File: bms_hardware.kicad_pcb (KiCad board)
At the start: 2 copper layers, 102 parts, among them J1 Conn_01x05_Male, J2 Conn_01x07_Female, Q1 2N7002, Q2 2N7002, Q3 2N7002, Q4 2N7002, Q5 2N7002, Q6 2N7002, U1 STM32F407VGTx, U2 BQ76PL536A, U3 INA226, Y1 8MHz

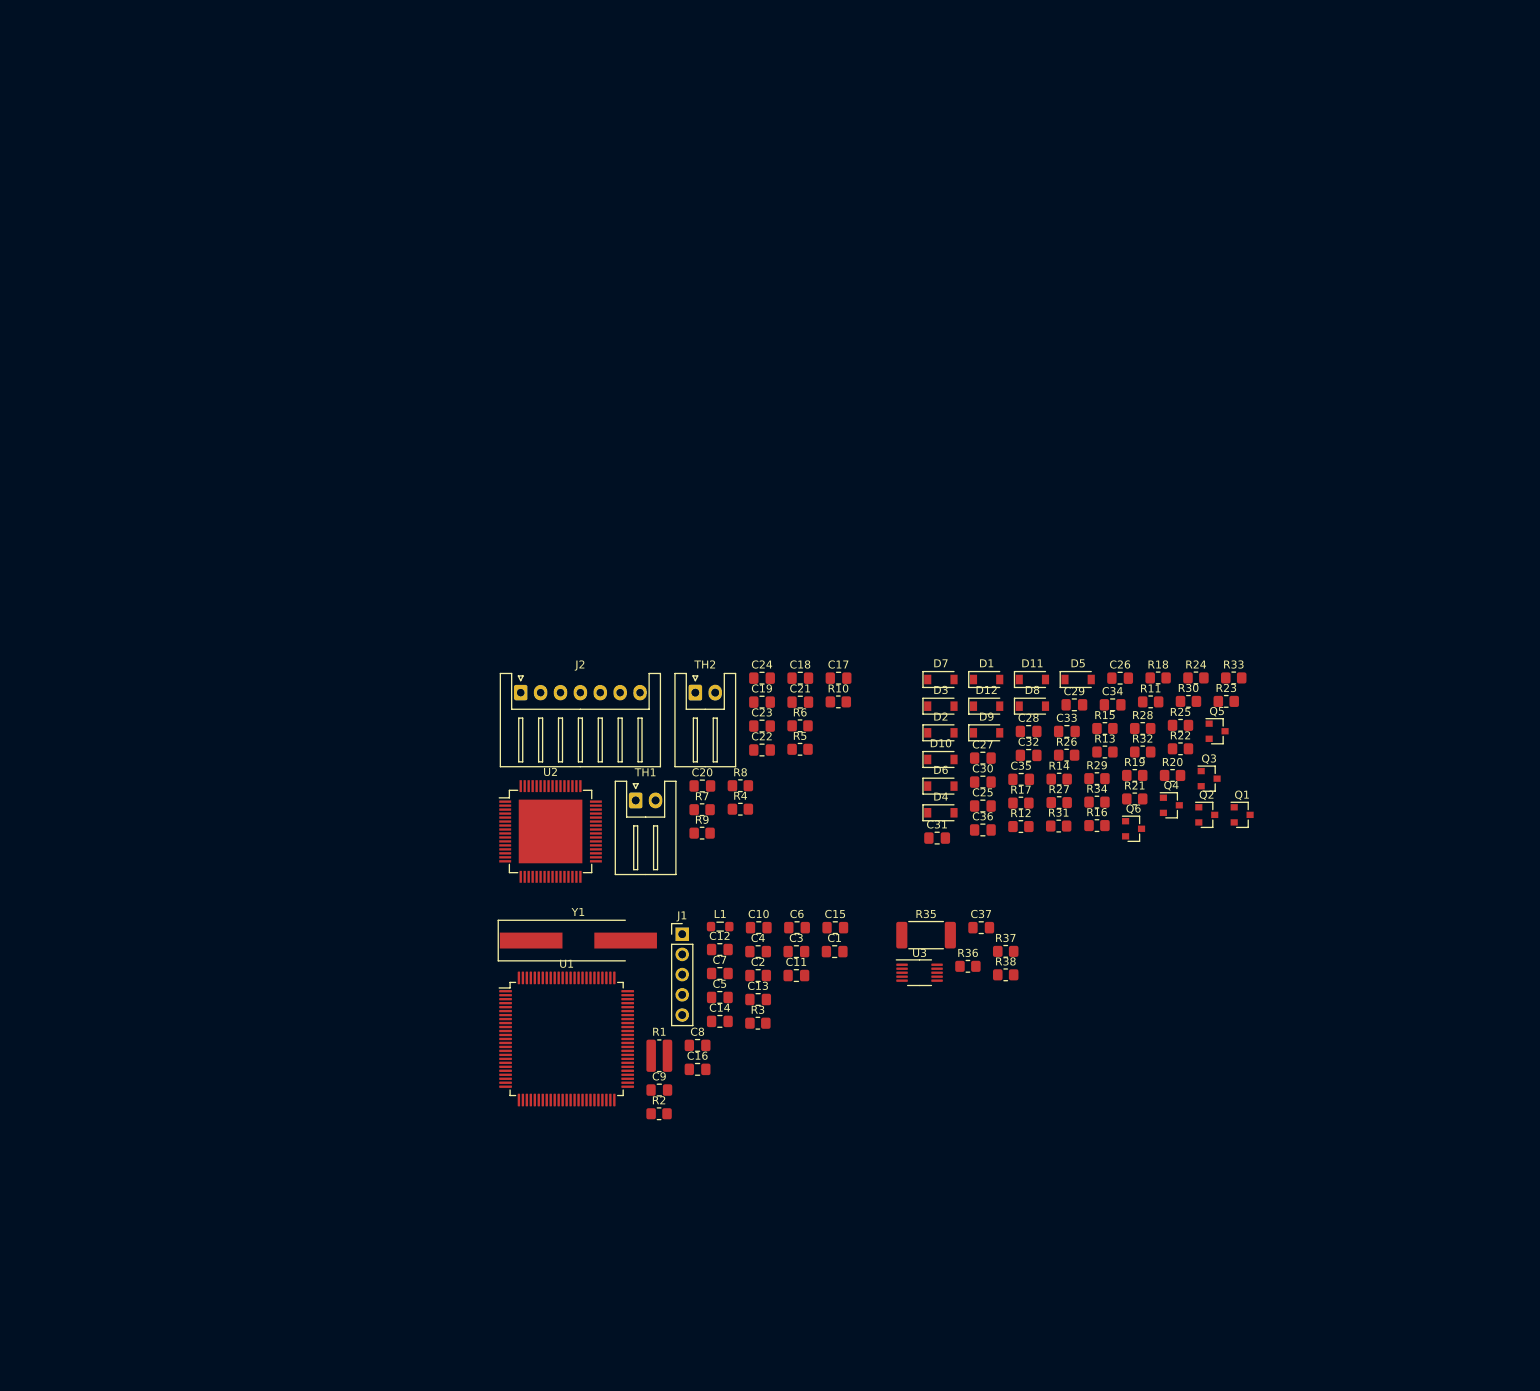
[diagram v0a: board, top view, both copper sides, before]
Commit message: Fixes missing footprints, adds initial pcb
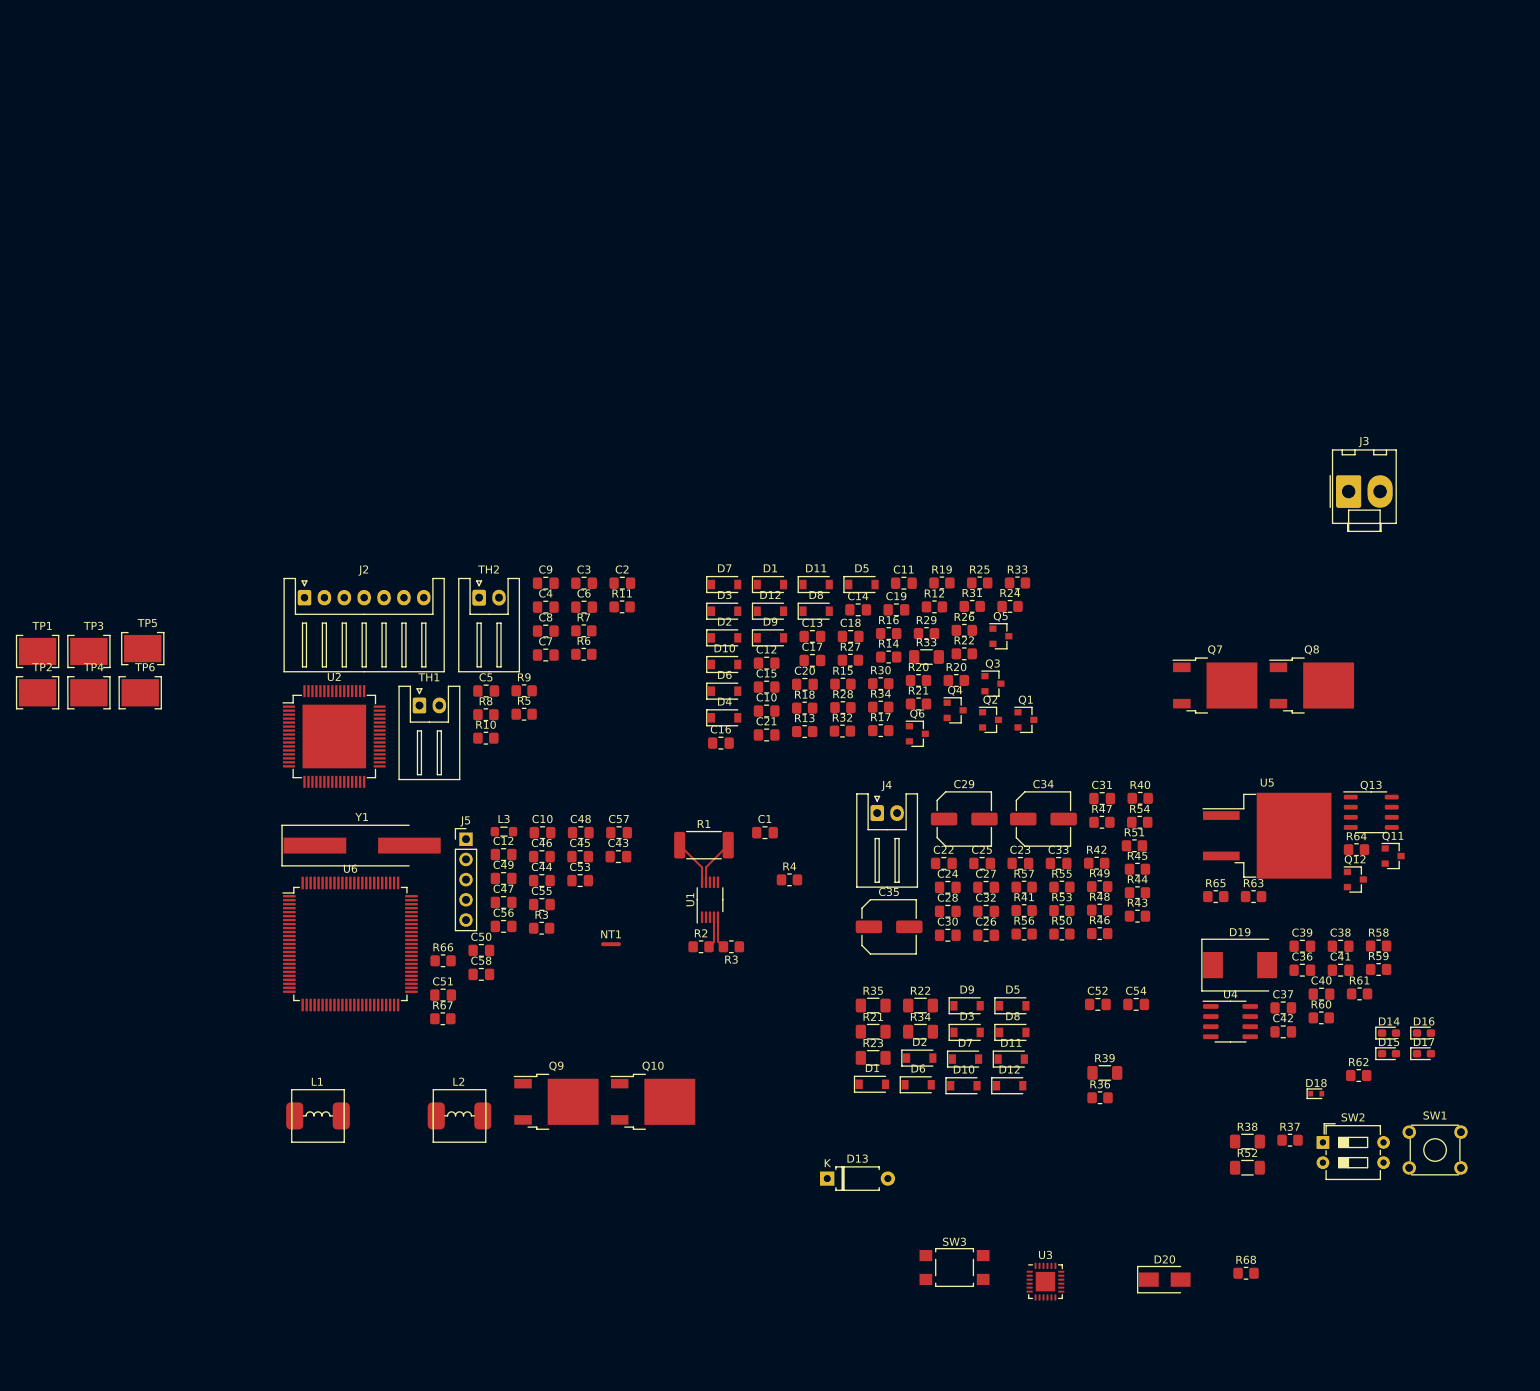
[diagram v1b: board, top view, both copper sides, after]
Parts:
- removed the R1 at (137.1, 113.1)
- removed the R32 at (197.9, 74.9)
- added C22: 1uF, Capacitor_SMD:C_0805_2012Metric_Pad1.18x1.45mm_HandSolder, F.Cu at (172.9, 88.9)
- added C23: 1uF, Capacitor_SMD:C_0805_2012Metric_Pad1.18x1.45mm_HandSolder, F.Cu at (182.5, 88.9)
- added C24: 2.7nF, Capacitor_SMD:C_0805_2012Metric_Pad1.18x1.45mm_HandSolder, F.Cu at (173.4, 91.9)
- added C25: 0.1uF, Capacitor_SMD:C_0805_2012Metric_Pad1.18x1.45mm_HandSolder, F.Cu at (177.7, 88.9)
- added C26: 0.1uF, Capacitor_SMD:C_0805_2012Metric_Pad1.18x1.45mm_HandSolder, F.Cu at (178.2, 97.9)
- added C27: 0.1uF, Capacitor_SMD:C_0805_2012Metric_Pad1.18x1.45mm_HandSolder, F.Cu at (178.2, 91.9)
- added C28: 0.056uF, Capacitor_SMD:C_0805_2012Metric_Pad1.18x1.45mm_HandSolder, F.Cu at (173.4, 94.9)
- added C29: 10uF, Capacitor_SMD:C_Elec_6.3x7.7, F.Cu at (175.5, 83.3)
- added C30: 1uF, Capacitor_SMD:C_0805_2012Metric_Pad1.18x1.45mm_HandSolder, F.Cu at (173.4, 97.9)
- added C31: 0.1uF, Capacitor_SMD:C_0805_2012Metric_Pad1.18x1.45mm_HandSolder, F.Cu at (192.8, 80.8)
- added C32: 0.1uF, Capacitor_SMD:C_0805_2012Metric_Pad1.18x1.45mm_HandSolder, F.Cu at (178.2, 94.9)
- added C33: 0.1uF, Capacitor_SMD:C_0805_2012Metric_Pad1.18x1.45mm_HandSolder, F.Cu at (187.3, 88.9)
- added C34: 10uF, Capacitor_SMD:C_Elec_6.3x7.7, F.Cu at (185.4, 83.3)
- added C35: 10uF, Capacitor_SMD:C_Elec_6.3x7.7, F.Cu at (166.0, 96.9)
- added C36: 3.3nF, Capacitor_SMD:C_0805_2012Metric_Pad1.18x1.45mm_HandSolder, F.Cu at (218.0, 102.3)
- added C37: 330nF, Capacitor_SMD:C_0805_2012Metric_Pad1.18x1.45mm_HandSolder, F.Cu at (215.6, 107.1)
- added C38: 10uF, Capacitor_SMD:C_0805_2012Metric_Pad1.18x1.45mm_HandSolder, F.Cu at (222.8, 99.3)
- added C39: 0.1uF, Capacitor_SMD:C_0805_2012Metric_Pad1.18x1.45mm_HandSolder, F.Cu at (218.0, 99.3)
- added C40: 2.2nF, Capacitor_SMD:C_0805_2012Metric_Pad1.18x1.45mm_HandSolder, F.Cu at (220.4, 105.3)
- added C41: 1nF, Capacitor_SMD:C_0805_2012Metric_Pad1.18x1.45mm_HandSolder, F.Cu at (222.8, 102.3)
- added C42: 10uF, Capacitor_SMD:C_0805_2012Metric_Pad1.18x1.45mm_HandSolder, F.Cu at (215.6, 110.1)
- added C52: 1uF, Capacitor_SMD:C_0805_2012Metric_Pad1.18x1.45mm_HandSolder, F.Cu at (192.3, 106.6)
- added C54: 100nF, Capacitor_SMD:C_0805_2012Metric_Pad1.18x1.45mm_HandSolder, F.Cu at (197.1, 106.6)
- added D1: BZT52, Diode_SMD:D_SOD-123, F.Cu at (163.9, 116.7)
- added D10: BZT52, Diode_SMD:D_SOD-123, F.Cu at (175.4, 116.9)
- added D11: BZT52, Diode_SMD:D_SOD-123, F.Cu at (181.4, 113.5)
- added D12: BZT52, Diode_SMD:D_SOD-123, F.Cu at (181.2, 116.9)
- added D13: N4007, Diode_THT:D_A-405_P7.62mm_Horizontal, F.Cu at (158.2, 128.5)
- added D14: VCC, LED_SMD:LED_0603_1608Metric_Pad1.05x0.95mm_HandSolder, F.Cu at (228.9, 110.2)
- added D15: PG, LED_SMD:LED_0603_1608Metric_Pad1.05x0.95mm_HandSolder, F.Cu at (228.9, 112.8)
- added D16: STAT2, LED_SMD:LED_0603_1608Metric_Pad1.05x0.95mm_HandSolder, F.Cu at (233.2, 110.2)
- added D17: STAT1, LED_SMD:LED_0603_1608Metric_Pad1.05x0.95mm_HandSolder, F.Cu at (233.2, 112.8)
- added D18: RB541SM-40FHT2R, Diode_SMD:D_SOD-523, F.Cu at (219.7, 117.9)
- added D19: B340, Diode_SMD:D_SMC, F.Cu at (210.1, 101.7)
- added D2: BZT52, Diode_SMD:D_SOD-123, F.Cu at (169.9, 113.4)
- added D20: D, Diode_SMD:D_SMA, F.Cu at (200.7, 141.2)
- added D3: BZT52, Diode_SMD:D_SOD-123, F.Cu at (175.8, 110.2)
- added D5: BZT52, Diode_SMD:D_SOD-123, F.Cu at (181.6, 106.8)
- added D6: BZT52, Diode_SMD:D_SOD-123, F.Cu at (169.7, 116.7)
- added D7: BZT52, Diode_SMD:D_SOD-123, F.Cu at (175.6, 113.5)
- added D8: BZT52, Diode_SMD:D_SOD-123, F.Cu at (181.6, 110.2)
- added D9: BZT52, Diode_SMD:D_SOD-123, F.Cu at (175.8, 106.8)
- added J3: Vcc In, Connector_Molex:Molex_KK-396_A-41791-0002_1x02_P3.96mm_Vertical, F.Cu at (223.8, 42.2)
- added J4: CH_TS, Connector_JST:JST_XH_S2B-XH-A_1x02_P2.50mm_Horizontal, F.Cu at (164.5, 82.6)
- added L1: 6.8uH, Inductor_SMD:L_BOURNS_SRP6030, F.Cu at (94.2, 120.7)
- added L2: 6.8uH, Inductor_SMD:L_BOURNS_SRP6030, F.Cu at (112.0, 120.7)
- added NT1: GND-TIE, NetTie:NetTie-3_SMD_Pad0.5mm, F.Cu at (131.1, 99.1)
- added Q10: FDD86580-F085, Package_TO_SOT_SMD:TO-252-2, F.Cu at (136.4, 118.9)
- added Q11: BC848, Package_TO_SOT_SMD:SOT-23, F.Cu at (229.4, 88.0)
- added Q12: BC848, Package_TO_SOT_SMD:SOT-23, F.Cu at (224.6, 90.9)
- added Q13: IRF9310PbF, Package_SO:SO-8_3.9x4.9mm_P1.27mm, F.Cu at (226.6, 82.5)
- added Q7: DMP4051LK3, Package_TO_SOT_SMD:TO-252-2, F.Cu at (207.0, 66.5)
- added Q8: DMP4051LK3, Package_TO_SOT_SMD:TO-252-2, F.Cu at (219.2, 66.5)
- added Q9: FDD86580-F085, Package_TO_SOT_SMD:TO-252-2, F.Cu at (124.2, 118.9)
- added R21: 47@1/2W, Resistor_SMD:R_1206_3216Metric_Pad1.30x1.75mm_HandSolder, F.Cu at (164.0, 110.1)
- added R22: 47@1/2W, Resistor_SMD:R_1206_3216Metric_Pad1.30x1.75mm_HandSolder, F.Cu at (170.0, 106.8)
- added R23: 47@1/2W, Resistor_SMD:R_1206_3216Metric_Pad1.30x1.75mm_HandSolder, F.Cu at (164.0, 113.4)
- added R33: 47@1/2W, Resistor_SMD:R_1206_3216Metric_Pad1.30x1.75mm_HandSolder, F.Cu at (170.7, 63.0)
- added R34: 47@1/2W, Resistor_SMD:R_1206_3216Metric_Pad1.30x1.75mm_HandSolder, F.Cu at (170.0, 110.1)
- added R35: 47@1/2W, Resistor_SMD:R_1206_3216Metric_Pad1.30x1.75mm_HandSolder, F.Cu at (164.0, 106.8)
- added R36: 10k 1/8W 5%, Resistor_SMD:R_0805_2012Metric_Pad1.20x1.40mm_HandSolder, F.Cu at (192.5, 118.4)
- added R37: 10R, Resistor_SMD:R_0805_2012Metric_Pad1.20x1.40mm_HandSolder, F.Cu at (216.4, 123.7)
- added R38: 6R2 1/4W 1%, Resistor_SMD:R_1206_3216Metric_Pad1.30x1.75mm_HandSolder, F.Cu at (211.1, 123.9)
- added R39: 0R010⁯ 1W 0.5%, Resistor_SMD:R_1206_3216Metric_Pad1.30x1.75mm_HandSolder, F.Cu at (193.1, 115.2)
- added R40: 10K, Resistor_SMD:R_0805_2012Metric_Pad1.20x1.40mm_HandSolder, F.Cu at (197.6, 80.7)
- added R41: 10K, Resistor_SMD:R_0805_2012Metric_Pad1.20x1.40mm_HandSolder, F.Cu at (183.0, 94.8)
- added R42: 100K, Resistor_SMD:R_0805_2012Metric_Pad1.20x1.40mm_HandSolder, F.Cu at (192.1, 88.9)
- added R43: 1K, Resistor_SMD:R_0805_2012Metric_Pad1.20x1.40mm_HandSolder, F.Cu at (197.2, 95.5)
- added R44: 5K6, Resistor_SMD:R_0805_2012Metric_Pad1.20x1.40mm_HandSolder, F.Cu at (197.2, 92.6)
- added R45: 470R, Resistor_SMD:R_0805_2012Metric_Pad1.20x1.40mm_HandSolder, F.Cu at (197.2, 89.6)
- added R46: 470R, Resistor_SMD:R_0805_2012Metric_Pad1.20x1.40mm_HandSolder, F.Cu at (192.5, 97.7)
- added R47: 470R, Resistor_SMD:R_0805_2012Metric_Pad1.20x1.40mm_HandSolder, F.Cu at (192.8, 83.7)
- added R48: 10K*, Resistor_SMD:R_0805_2012Metric_Pad1.20x1.40mm_HandSolder, F.Cu at (192.5, 94.8)
- added R49: 10K*, Resistor_SMD:R_0805_2012Metric_Pad1.20x1.40mm_HandSolder, F.Cu at (192.5, 91.8)
- added R50: 37K*, Resistor_SMD:R_0805_2012Metric_Pad1.20x1.40mm_HandSolder, F.Cu at (187.7, 97.8)
- added R51: 8K2*, Resistor_SMD:R_0805_2012Metric_Pad1.20x1.40mm_HandSolder, F.Cu at (196.9, 86.7)
- added R52: 0R020 1W 0.5%, Resistor_SMD:R_1206_3216Metric_Pad1.30x1.75mm_HandSolder, F.Cu at (211.1, 127.2)
- added R53: 6K8*, Resistor_SMD:R_0805_2012Metric_Pad1.20x1.40mm_HandSolder, F.Cu at (187.7, 94.8)
- added R54: 10K*, Resistor_SMD:R_0805_2012Metric_Pad1.20x1.40mm_HandSolder, F.Cu at (197.5, 83.7)
- added R55: 1K 1/8W 1%, Resistor_SMD:R_0805_2012Metric_Pad1.20x1.40mm_HandSolder, F.Cu at (187.7, 91.9)
- added R56: 560K 1/10W 0.5%, Resistor_SMD:R_0805_2012Metric_Pad1.20x1.40mm_HandSolder, F.Cu at (183.0, 97.8)
- added R57: 51K 1/8W 0.5%, Resistor_SMD:R_0805_2012Metric_Pad1.20x1.40mm_HandSolder, F.Cu at (183.0, 91.9)
- added R58: 330K, Resistor_SMD:R_0805_2012Metric_Pad1.20x1.40mm_HandSolder, F.Cu at (227.5, 99.3)
- added R59: 27K, Resistor_SMD:R_0805_2012Metric_Pad1.20x1.40mm_HandSolder, F.Cu at (227.5, 102.2)
- added R60: 9K1, Resistor_SMD:R_0805_2012Metric_Pad1.20x1.40mm_HandSolder, F.Cu at (220.3, 108.3)
- added R61: 1K8, Resistor_SMD:R_0805_2012Metric_Pad1.20x1.40mm_HandSolder, F.Cu at (225.1, 105.3)
- added R62: 5K1, Resistor_SMD:R_0805_2012Metric_Pad1.20x1.40mm_HandSolder, F.Cu at (225.0, 115.6)
- added R63: 3.3K, Resistor_SMD:R_0805_2012Metric_Pad1.20x1.40mm_HandSolder, F.Cu at (211.8, 93.1)
- added R64: 33K, Resistor_SMD:R_0805_2012Metric_Pad1.20x1.40mm_HandSolder, F.Cu at (224.8, 87.2)
- added R65: 22K, Resistor_SMD:R_0805_2012Metric_Pad1.20x1.40mm_HandSolder, F.Cu at (207.1, 93.1)
- added R66: 220, Resistor_SMD:R_0805_2012Metric_Pad1.20x1.40mm_HandSolder, F.Cu at (110.0, 101.1)
- added R68: 47, Resistor_SMD:R_0805_2012Metric_Pad1.20x1.40mm_HandSolder, F.Cu at (210.9, 140.4)
- added SW1: Reset, Button_Switch_THT:SW_TH_Tactile_Omron_B3F-10xx, F.Cu at (231.4, 122.7)
- added SW2: Select CE, Button_Switch_THT:SW_DIP_SPSTx02_Slide_6.7x6.64mm_W7.62mm_P2.54mm_LowProfile, F.Cu at (220.5, 124.0)
- added SW3: SW_Push, Button_Switch_SMD:SW_SPST_TL3305A, F.Cu at (174.2, 139.7)
- added TP1: GND_BAT, TestPoint:KEYSTONE_5016, F.Cu at (59.0, 62.3)
- added TP2: GNDA, TestPoint:KEYSTONE_5016, F.Cu at (59.0, 67.5)
- added TP3: VREF, TestPoint:KEYSTONE_5016, F.Cu at (65.4, 62.3)
- added TP4: VBUS, TestPoint:KEYSTONE_5016, F.Cu at (65.4, 67.5)
- added TP5: VCC, TestPoint:KEYSTONE_5016, F.Cu at (72.2, 61.9)
- added TP6: CH_BAT, TestPoint:KEYSTONE_5016, F.Cu at (71.9, 67.5)
- added U3: BQ24618RGET, Package_DFN_QFN:VQFN-24-1EP_4x4mm_P0.5mm_EP2.45x2.45mm, F.Cu at (185.7, 141.5)
- added U4: TPS54331D, Package_SO:SOIC-8_3.9x4.9mm_P1.27mm, F.Cu at (208.9, 108.8)
- added U5: FERD2045SB-TR, Package_TO_SOT_SMD:TO-263-2_TabPin1, F.Cu at (213.5, 85.4)
- C13: renamed from C28; value C -> 0.1uF
- C14: renamed from C29; value C -> 0.1uF
- C15: renamed from C30; value C -> 0.1uF
- C19: renamed from C34; value C -> 0.1uF
- C20: renamed from C35; value C -> 0.1uF
- C21: renamed from C36; value C -> 0.1uF
- C58: renamed from C16; value 1uF -> 10uF
- D4: value D_Zener -> BZT52
- L3: renamed from L1; value L -> fcd0805
- R15: renamed from R14; value R -> 1K
- R16: renamed from R15; value R -> 1K
- R17: renamed from R16; value R -> 1K
- R18: renamed from R17; value R -> 1M
- R19: renamed from R18; value R -> 1M
- R20: renamed from R19; value R -> 1M
- R27: renamed from R26; value R -> 1K
- R28: renamed from R27; value R -> 1K
- R29: renamed from R28; value R -> 1K
- R30: renamed from R29; value R -> 1M
- R31: renamed from R30; value R -> 1M
- R32: renamed from R31; value R -> 1M
- moved R3 34.5 mm to (146.2, 99.4), turned to 180 degrees
- moved R2 33.6 mm to (142.4, 99.4)
- moved R1 30.1 mm to (142.7, 86.6)
- moved C4 29.7 mm to (122.9, 56.7)
- moved C45 29.7 mm to (127.2, 88.1)
- moved C7 29.7 mm to (122.9, 62.7)
- moved C8 29.7 mm to (122.9, 59.7)
- moved C9 29.7 mm to (122.9, 53.7)
- moved J5 29.7 mm to (112.8, 85.9)
- moved R10 29.7 mm to (115.3, 73.2)
- moved R8 29.7 mm to (115.3, 70.2)
- moved C5 29.7 mm to (115.4, 67.2)
- moved C53 29.7 mm to (127.2, 91.1)
- moved C14 29.7 mm to (162.1, 57.0)
- moved C19 29.7 mm to (166.9, 57.0)
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- renumbered C37 to C1, C25 to C10, C26 to C11, C27 to C12, C31 to C16, C32 to C17, C33 to C18, C17 to C2, C18 to C3, C19 to C4, C1 to C43, C2 to C44, C3 to C45, C4 to C46, C5 to C47, C6 to C48, C7 to C49, C20 to C5, C8 to C50, C9 to C51, C11 to C53, C13 to C55, C14 to C56, C15 to C57, C21 to C6, C22 to C7, C23 to C8, C24 to C9, J1 to J5, R35 to R1, R9 to R10, R10 to R11, R11 to R12, R12 to R13, R13 to R14, R36 to R2, R23 to R24, R24 to R25, R25 to R26, R37 to R3, R38 to R4, R4 to R5, R5 to R6, R2 to R67, R6 to R7, R7 to R8, R8 to R9, U3 to U1, U1 to U6
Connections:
- net /current_sensor_ina226/ALERT renamed /current_sensor_ina226/ALERT_INA226
- net Net-(U1-Pad70) renamed /mcu_stm32f407/CAN_1RX
- net Net-(U1-Pad71) renamed /mcu_stm32f407/CAN_1TX
- R1 pad 1: /current_sensor_ina226/IN+ -> +24V
- R1 pad 2: +24V -> /bat_switch/D
- R5 pad 1: /equalizer_bq76/SCLK -> /mcu_stm32f407/SCK
- R6 pad 1: /equalizer_bq76/SDI -> /mcu_stm32f407/MOSI
- R7 pad 1: /equalizer_bq76/CONV -> /mcu_stm32f407/BQ76_CONV
- U1 pad 10: /current_sensor_ina226/IN+ -> +24V
- U1 pad 8: /current_sensor_ina226/V_BATT -> +24V
- U1 pad 9: +24V -> /bat_switch/D
- U2 pad 36: /equalizer_bq76/CONV -> /mcu_stm32f407/BQ76_CONV
- U2 pad 37: /equalizer_bq76/DRDY -> /mcu_stm32f407/BQ76_DRDY
- U2 pad 38: /equalizer_bq76/ALERT -> /equalizer_bq76/ALERT_BQ76
- U2 pad 39: /equalizer_bq76/FAULT -> /mcu_stm32f407/BQ76_FAULT
- U2 pad 40: /equalizer_bq76/SCLK -> /mcu_stm32f407/SCK
- U2 pad 41: /equalizer_bq76/SDO -> /mcu_stm32f407/MISO
- U2 pad 42: /equalizer_bq76/SDI -> /mcu_stm32f407/MOSI
- U6 pad 29: Net-(U1-Pad29) -> /equalizer_bq76/CS
- U6 pad 30: Net-(U1-Pad30) -> /mcu_stm32f407/SCK
- U6 pad 31: Net-(U1-Pad31) -> /mcu_stm32f407/MISO
- U6 pad 32: Net-(U1-Pad32) -> /mcu_stm32f407/MOSI
- U6 pad 33: Net-(U1-Pad33) -> /mcu_stm32f407/BQ76_FAULT
- U6 pad 34: Net-(U1-Pad34) -> /equalizer_bq76/ALERT_BQ76
- U6 pad 37: Net-(U1-Pad37) -> GND
- U6 pad 63: Net-(U1-Pad63) -> /mcu_stm32f407/BQ76_DRDY
- U6 pad 64: Net-(U1-Pad64) -> /mcu_stm32f407/BQ76_CONV
- U6 pad 91: Net-(U1-Pad91) -> /bat_switch/G
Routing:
- net +24V: track 0.00 -> 5.82 mm
- net /bat_switch/D: track 0.00 -> 5.81 mm
- net /current_sensor_ina226/SCL: track 0.00 -> 4.00 mm
- net /current_sensor_ina226/SDA: track 0.00 -> 3.98 mm

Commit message: Adds pcb file
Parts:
- removed the C10 at (122.5, 85.0)
- removed the C12 at (117.6, 87.8)
- removed the D1 at (151.1, 53.9)
- removed the D10 at (145.3, 63.9)
- removed the D11 at (156.8, 53.9)
- removed the D12 at (151.1, 57.2)
- removed the D12 at (181.2, 116.9)
- removed the D2 at (145.3, 60.6)
- removed the D3 at (145.3, 57.2)
- removed the D5 at (162.6, 53.9)
- removed the D6 at (145.3, 67.3)
- removed the D7 at (145.3, 53.9)
- removed the D8 at (156.8, 57.2)
- removed the D9 at (151.1, 60.6)
- removed the R20 at (174.5, 65.9)
- removed the R21 at (169.7, 68.9)
- removed the R22 at (175.5, 62.6)
- removed the R22 at (170.0, 106.8)
- removed the R3 at (122.3, 97.1)
- removed the R3 at (146.2, 99.4)
- removed the R33 at (182.2, 53.7)
- removed the R34 at (165.0, 69.3)
- removed R5, R6, R7: 10K, Resistor_SMD:R_0805_2012Metric_Pad1.20x1.40mm_HandSolder
- removed TP1: GND_BAT, TestPoint:KEYSTONE_5016
- removed TP2: GNDA, TestPoint:KEYSTONE_5016
- removed TP3: VREF, TestPoint:KEYSTONE_5016
- removed TP4: VBUS, TestPoint:KEYSTONE_5016
- removed TP5: VCC, TestPoint:KEYSTONE_5016
- removed TP6: CH_BAT, TestPoint:KEYSTONE_5016
- added D12: BZT52, Diode_SMD:D_SOD-123, B.Cu at (101.5, 112.5)
- added R22: 47@1/2W, Resistor_SMD:R_1206_3216Metric_Pad1.30x1.75mm_HandSolder, F.Cu at (103.3, 93.4)
- added R3: 10K, Resistor_SMD:R_0805_2012Metric_Pad1.20x1.40mm_HandSolder, F.Cu at (181.1, 105.0)
- C10, C11, C12, C13, C14, C15, C16, C17, C18, C19, C20, C21, C4, C47, C49, C7, D10, D11, D4, D5, D6, L3, R10, R11, R12, R13, R14, R24, R25, R26, R8, R9: moved to B.Cu
- U5: footprint Package_TO_SOT_SMD:TO-263-2_TabPin1 -> Package_TO_SOT_SMD:TO-263-3_TabPin2
- Y1: footprint Crystal:Crystal_SMD_HC49-SD_HandSoldering -> Crystal:Crystal_SMD_HC49-SD
- moved D20 148.6 mm to (138.5, 6.29)
- moved R65 145.0 mm to (100.8, -5.57)
- moved Q12 145.0 mm to (118.3, -7.72)
- moved R64 145.0 mm to (118.5, -11.5)
- moved Q11 142.3 mm to (130.2, -14.1)
- moved R63 132.3 mm to (134.1, -14.0), turned to 270 degrees
- moved SW1 122.6 mm to (173.1, 14.8), turned to 180 degrees
- moved L1 121.3 mm to (214.9, 108.7)
- moved Q13 117.1 mm to (156.3, -11.1)
- moved SW2 115.0 mm to (173.1, 19.2), turned to 270 degrees
- moved Q9 102.4 mm to (223.4, 93.3)
- moved U5 102.3 mm to (156.3, 0.64), turned to 270 degrees
- moved C58 90.8 mm to (185.1, 45.4)
- moved Q10 89.0 mm to (223.4, 100.3)
- moved R25 88.4 mm to (106.8, 106.7)
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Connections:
- J2 pad 1: GND -> +24V
- J2 pad 2: /equalizer_bq76/balancing_module/CELL_1+ -> /equalizer_bq76/balancing_module/CELL_5+
- J2 pad 3: /equalizer_bq76/balancing_module/CELL_2+ -> /equalizer_bq76/balancing_module/CELL_4+
- J2 pad 5: /equalizer_bq76/balancing_module/CELL_4+ -> /equalizer_bq76/balancing_module/CELL_2+
- J2 pad 6: /equalizer_bq76/balancing_module/CELL_5+ -> /equalizer_bq76/balancing_module/CELL_1+
- J2 pad 7: +24V -> GND
- U6 pad 35: Net-(U6-Pad35) -> /mcu_stm32f407/BQ76_DRDY
- U6 pad 36: Net-(U6-Pad36) -> /mcu_stm32f407/BQ76_CONV
- U6 pad 63: /mcu_stm32f407/BQ76_DRDY -> Net-(U6-Pad63)
- U6 pad 64: /mcu_stm32f407/BQ76_CONV -> Net-(U6-Pad64)
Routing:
- net VBAT: track 0.00 -> 120.5 mm, vias 0 -> 1
- net REG50: track 0.00 -> 113.6 mm, vias 0 -> 1
- net GND: track 0.00 -> 96.7 mm
- net +24V: track 5.82 -> 86.3 mm
- net Net-(C27-Pad2): track 0.00 -> 56.4 mm
- net NRST: track 0.00 -> 51.3 mm, vias 0 -> 2
- net /equalizer_bq76/balancing_module/CELL_1+: track 0.00 -> 40.1 mm
- net /bat_charger/ACP: track 0.00 -> 39.2 mm
- net /equalizer_bq76/balancing_module/CELL_5+: track 0.00 -> 38.1 mm
- net /equalizer_bq76/balancing_module/CELL_4+: track 0.00 -> 37.7 mm
- net /equalizer_bq76/balancing_module/CELL_2+: track 0.00 -> 37.7 mm
- net /equalizer_bq76/balancing_module/CELL_3+: track 0.00 -> 36.3 mm
- net /bat_charger/ACN: track 0.00 -> 32.3 mm
- net /bat_charger/PH: track 0.00 -> 32.1 mm
- net Net-(R8-Pad1): track 0.00 -> 28.2 mm
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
